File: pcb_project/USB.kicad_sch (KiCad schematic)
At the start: 6 parts, among them J2 USB_B_Mini, U2 TPS2041B

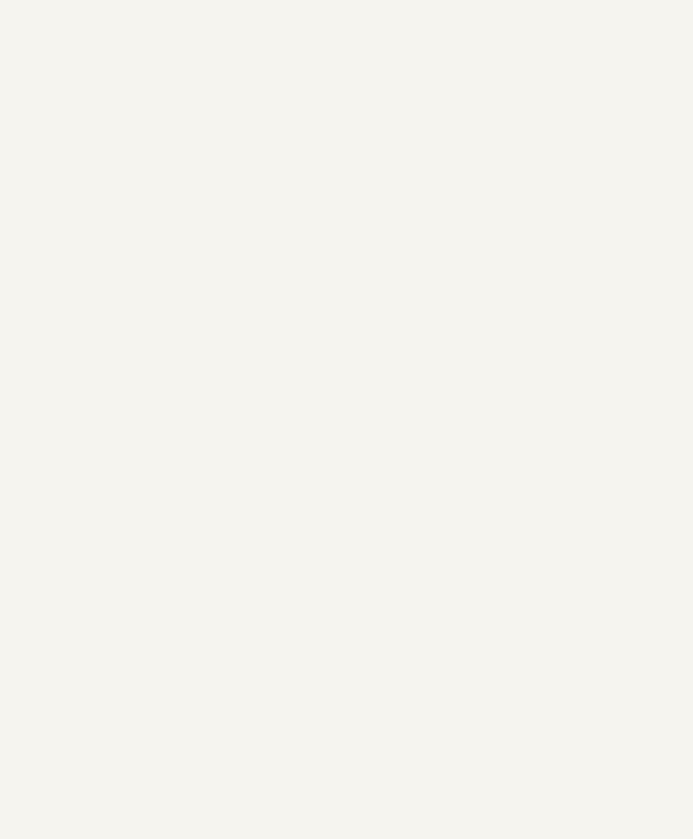
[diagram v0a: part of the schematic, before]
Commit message: Update USB circuits
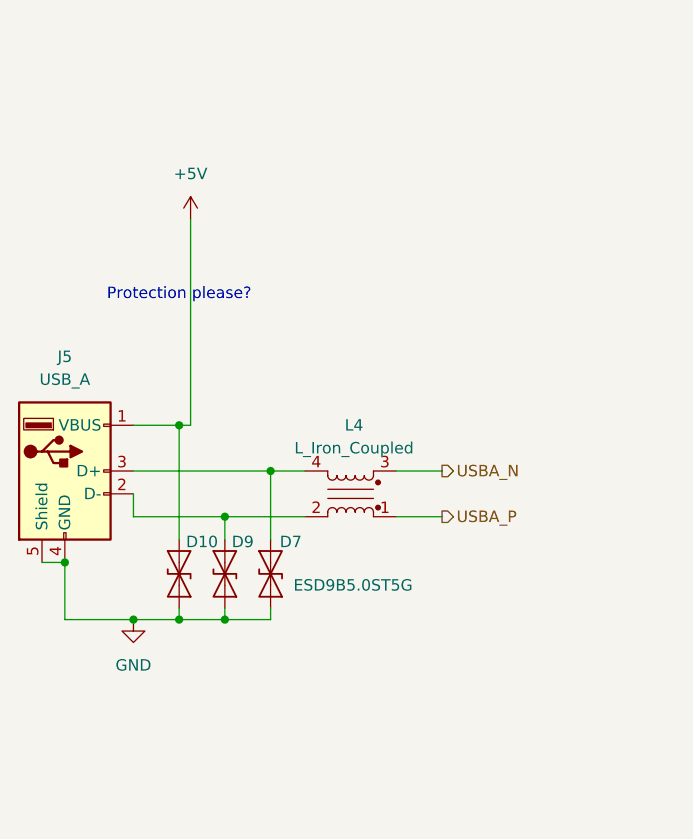
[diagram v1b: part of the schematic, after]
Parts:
- added D10, D7, D9: ESD9B5.0ST5G, Diode_SMD:D_SOD-923, symbol Diode:ESD9B5.0ST5G
- added J5: USB_A, symbol Connector:USB_A
- added L4: L_Iron_Coupled, symbol Device:L_Iron_Coupled
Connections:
- net GND: now also D10.1 (A1), D7.1 (A1), D9.1 (A1), J5.4 (GND), J5.5 (Shield)
- new net: D9.2 (A2), J5.2 (D-), L4.2
- new net: D7.2 (A2), J5.3 (D+), L4.4
- new net +5V: D10.2 (A2), J5.1 (VBUS)
- new net USBA_N: L4.3
- new net USBA_P: L4.1
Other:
- note added: "Protection please?"

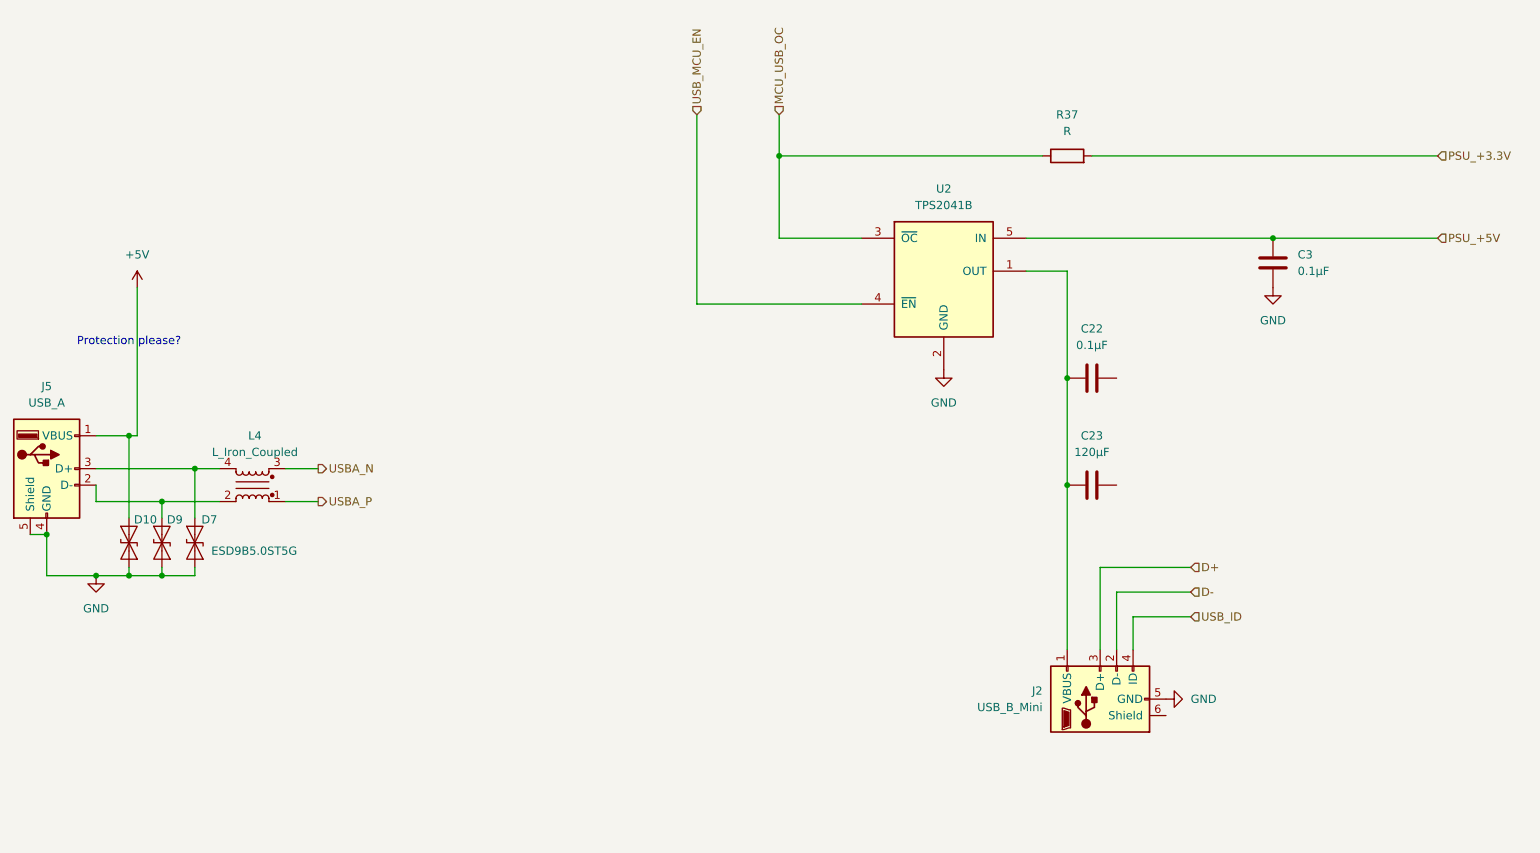
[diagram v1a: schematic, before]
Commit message: Update USB component and redo pin choices for MCU
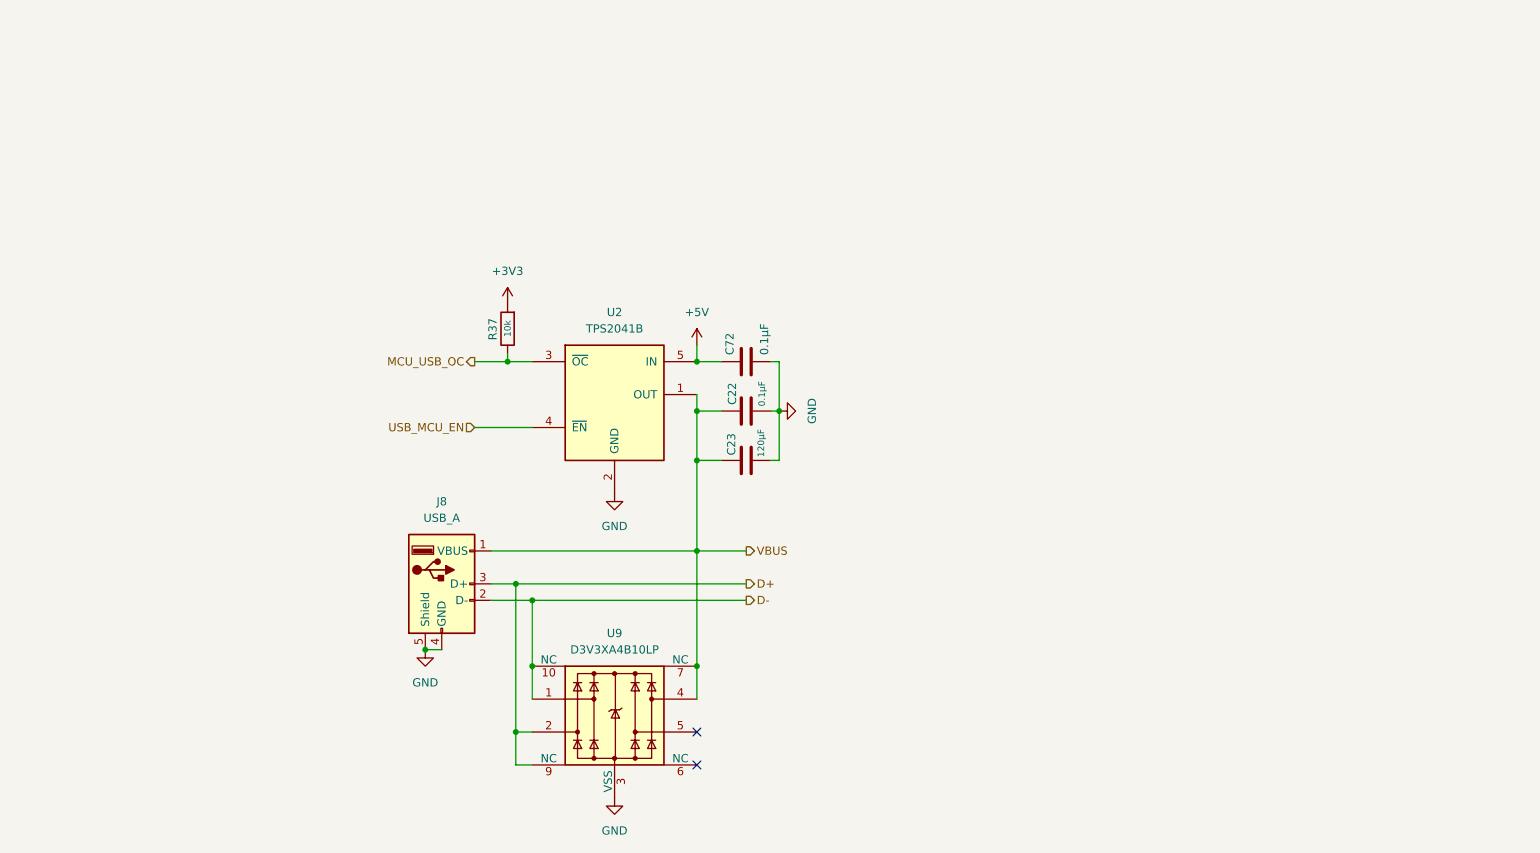
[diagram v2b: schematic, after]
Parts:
- removed C3: 0.1µF, symbol Device:C
- removed D10, D7, D9: ESD9B5.0ST5G, Diode_SMD:D_SOD-923, symbol Diode:ESD9B5.0ST5G
- removed J2: USB_B_Mini, symbol Connector:USB_B_Mini
- removed J5: USB_A, symbol Connector:USB_A
- removed L4: L_Iron_Coupled, symbol Device:L_Iron_Coupled
- added C72: 0.1μF, symbol Device:C
- added J8: USB_A, symbol Connector:USB_A
- added U9: D3V3XA4B10LP, Package_DFN_QFN:Diodes_UDFN-10_1.0x2.5mm_P0.5mm, symbol Power_Protection:D3V3XA4B10LP
- R37: value R -> 10k
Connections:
- net PSU_+5V is gone; now on net +5V: U2.5 (IN)
- net +5V: now also C72.1
- net D+: now also J8.3 (D+), U9.2, U9.9 (NC)
- net D-: now also J8.2 (D-), U9.1, U9.10 (NC)
- net GND: now also C22.1, C23.1, C72.2, J8.4 (GND), J8.5 (Shield), U9.3 (VSS), U9.8 (VSS)
- net VBUS: now reaches C22.2, C23.2, U2.1 (OUT)
- net VBUS: now also J8.1 (VBUS), U9.4, U9.7 (NC)
- net PSU_+3.3V renamed +3V3
- no-connect marks 0 -> 2
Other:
- note removed: "Protection please?"
- moved on the sheet: C22, C23, R37, U2

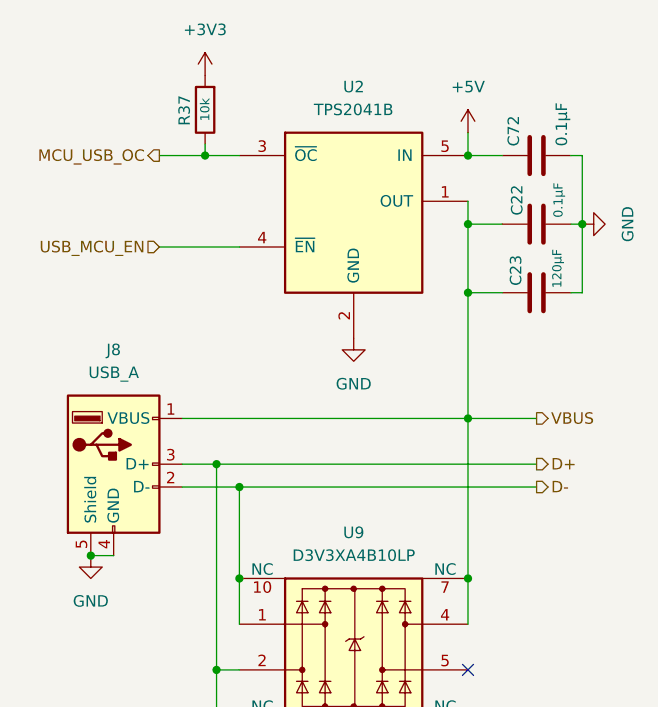
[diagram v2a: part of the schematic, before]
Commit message: ERC fixes, some remain
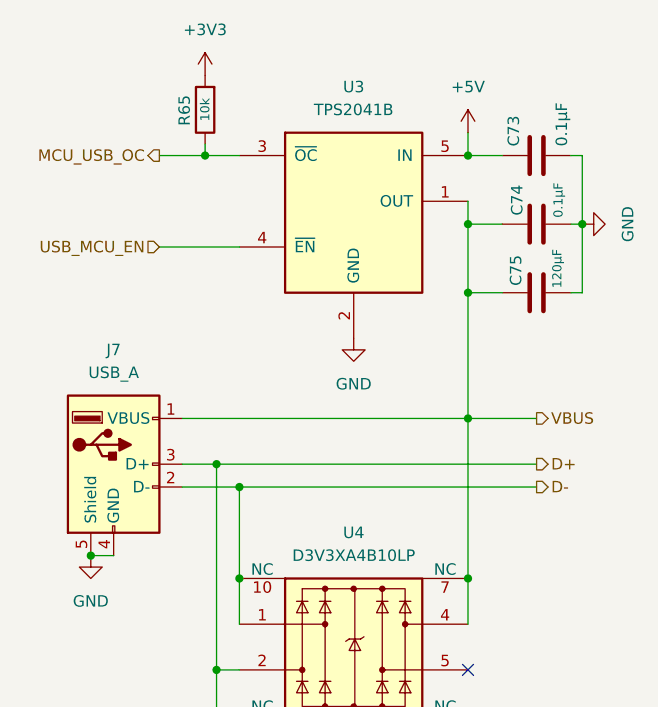
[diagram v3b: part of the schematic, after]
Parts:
- renumbered C72 to C73, C22 to C74, C23 to C75, J8 to J7, R37 to R65, U2 to U3, U9 to U4
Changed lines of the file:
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@@
 		(on_board yes)
 		(dnp no)
-		(property "Reference" "C22"
+		(property "Reference" "C74"
 			(at 145.161 74.803 0)
 			(effects
@@
 			(project ""
 				(path "/98f80f66-4595-4d0f-90ca-59b2db6f447b/d8354ada-74b3-4c6a-8679-c8f4ff1d8cd0"
-					(reference "C22")
+					(reference "C74")
 					(unit 1)
 				)
@@
 		(dnp no)
 		(fields_autoplaced yes)
-		(property "Reference" "#PWR011"
+		(property "Reference" "#PWR082"
 			(at 127 143.51 0)
 			(effects
@@
 			(project "pcb_project"
 				(path "/98f80f66-4595-4d0f-90ca-59b2db6f447b/d8354ada-74b3-4c6a-8679-c8f4ff1d8cd0"
-					(reference "#PWR011")
+					(reference "#PWR082")
 					(unit 1)
 				)
@@
 		(dnp no)
 		(fields_autoplaced yes)
-		(property "Reference" "U9"
+		(property "Reference" "U4"
 			(at 127 111.76 0)
 			(effects
@@
 			(project ""
 				(path "/98f80f66-4595-4d0f-90ca-59b2db6f447b/d8354ada-74b3-4c6a-8679-c8f4ff1d8cd0"
-					(reference "U9")
+					(reference "U4")
 					(unit 1)
 				)
@@
 		(on_board yes)
 		(dnp no)
-		(property "Reference" "R37"
+		(property "Reference" "R65"
 			(at 108.204 66.548 90)
 			(effects
@@
 			(project ""
 				(path "/98f80f66-4595-4d0f-90ca-59b2db6f447b/d8354ada-74b3-4c6a-8679-c8f4ff1d8cd0"
-					(reference "R37")
+					(reference "R65")
 					(unit 1)
 				)
@@
 		(dnp no)
 		(fields_autoplaced yes)
-		(property "Reference" "J8"
+		(property "Reference" "J7"
 			(at 100.33 91.44 0)
 			(effects
@@
 			(project "pcb_project"
 				(path "/98f80f66-4595-4d0f-90ca-59b2db6f447b/d8354ada-74b3-4c6a-8679-c8f4ff1d8cd0"
-					(reference "J8")
+					(reference "J7")
 					(unit 1)
 				)
@@
 		(on_board yes)
 		(dnp no)
-		(property "Reference" "C23"
+		(property "Reference" "C75"
 			(at 145.034 84.328 0)
 			(effects
@@
 			(project ""
 				(path "/98f80f66-4595-4d0f-90ca-59b2db6f447b/d8354ada-74b3-4c6a-8679-c8f4ff1d8cd0"
-					(reference "C23")
+					(reference "C75")
 					(unit 1)
 				)
@@
 		(dnp no)
 		(fields_autoplaced yes)
-		(property "Reference" "#PWR086"
+		(property "Reference" "#PWR079"
 			(at 97.79 120.65 0)
 			(effects
@@
 			(project "pcb_project"
 				(path "/98f80f66-4595-4d0f-90ca-59b2db6f447b/d8354ada-74b3-4c6a-8679-c8f4ff1d8cd0"
-					(reference "#PWR086")
+					(reference "#PWR079")
 					(unit 1)
 				)
@@
 		(dnp no)
 		(fields_autoplaced yes)
-		(property "Reference" "#PWR015"
+		(property "Reference" "#PWR084"
 			(at 158.75 77.47 0)
 			(effects
@@
 			(project "pcb_project"
 				(path "/98f80f66-4595-4d0f-90ca-59b2db6f447b/d8354ada-74b3-4c6a-8679-c8f4ff1d8cd0"
-					(reference "#PWR015")
+					(reference "#PWR084")
 					(unit 1)
 				)
@@
 		(dnp no)
 		(fields_autoplaced yes)
-		(property "Reference" "#PWR084"
+		(property "Reference" "#PWR083"
 			(at 139.7 71.12 0)
 			(effects
@@
 			(project ""
 				(path "/98f80f66-4595-4d0f-90ca-59b2db6f447b/d8354ada-74b3-4c6a-8679-c8f4ff1d8cd0"
-					(reference "#PWR084")
+					(reference "#PWR083")
 					(unit 1)
 				)
@@
 		(dnp no)
 		(fields_autoplaced yes)
-		(property "Reference" "#PWR013"
+		(property "Reference" "#PWR080"
 			(at 110.49 64.77 0)
 			(effects
@@
 			(project ""
 				(path "/98f80f66-4595-4d0f-90ca-59b2db6f447b/d8354ada-74b3-4c6a-8679-c8f4ff1d8cd0"
-					(reference "#PWR013")
+					(reference "#PWR080")
 					(unit 1)
 				)
@@
 		(on_board yes)
 		(dnp no)
-		(property "Reference" "C72"
+		(property "Reference" "C73"
 			(at 144.78 68.834 0)
 			(effects
@@
 			(project ""
 				(path "/98f80f66-4595-4d0f-90ca-59b2db6f447b/d8354ada-74b3-4c6a-8679-c8f4ff1d8cd0"
-					(reference "C72")
+					(reference "C73")
 					(unit 1)
 				)
@@
 		(dnp no)
 		(fields_autoplaced yes)
-		(property "Reference" "#PWR012"
+		(property "Reference" "#PWR081"
 			(at 127 96.52 0)
 			(effects
@@
 			(project ""
 				(path "/98f80f66-4595-4d0f-90ca-59b2db6f447b/d8354ada-74b3-4c6a-8679-c8f4ff1d8cd0"
-					(reference "#PWR012")
+					(reference "#PWR081")
 					(unit 1)
 				)
@@
 		(dnp no)
 		(fields_autoplaced yes)
-		(property "Reference" "U2"
+		(property "Reference" "U3"
 			(at 127 62.23 0)
 			(effects
@@
 			(project ""
 				(path "/98f80f66-4595-4d0f-90ca-59b2db6f447b/d8354ada-74b3-4c6a-8679-c8f4ff1d8cd0"
-					(reference "U2")
-					(unit 1)
-				)
+					(reference "U3")
+					(unit 1)
+				)

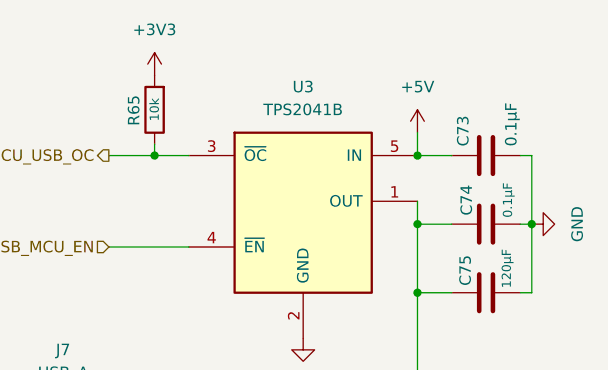
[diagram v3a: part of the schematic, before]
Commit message: Fix USB pins and other ERC errors
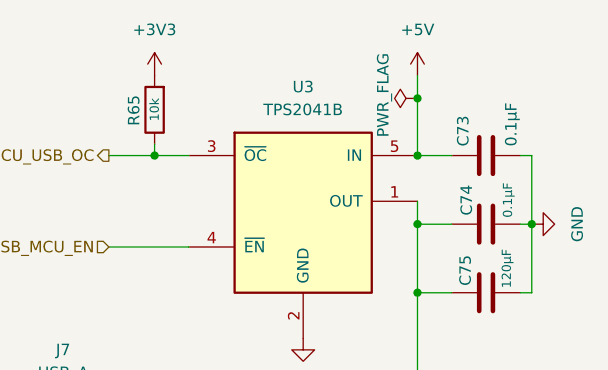
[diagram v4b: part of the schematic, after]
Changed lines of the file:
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@@
+	)
+	(junction
+		(at 139.7 63.5)
+		(diameter 0)
+		(color 0 0 0 0)
 	)
 	(junction
@@
 	(wire
 		(pts
-			(xy 139.7 67.31) (xy 139.7 69.85)
+			(xy 139.7 60.96) (xy 139.7 63.5)
 		)
 		(stroke
@@
 		(pts
 			(xy 111.76 127) (xy 111.76 132.08)
+		)
+		(stroke
+			(width 0)
+			(type default)
+		)
+	)
+	(wire
+		(pts
+			(xy 139.7 63.5) (xy 139.7 69.85)
 		)
 		(stroke
@@
 	(symbol
 		(lib_id "power:+5V")
-		(at 139.7 67.31 0)
+		(at 139.7 60.96 0)
 		(unit 1)
 		(exclude_from_sim no)
@@
 		(fields_autoplaced yes)
 		(property "Reference" "#PWR083"
-			(at 139.7 71.12 0)
+			(at 139.7 64.77 0)
 			(effects
 				(font
@@
 		)
 		(property "Value" "+5V"
-			(at 139.7 62.23 0)
+			(at 139.7 55.88 0)
 			(effects
 				(font
@@
 		)
 		(property "Footprint" ""
-			(at 139.7 67.31 0)
+			(at 139.7 60.96 0)
 			(effects
 				(font
@@
 		)
 		(property "Datasheet" ""
-			(at 139.7 67.31 0)
+			(at 139.7 60.96 0)
 			(effects
 				(font
@@
 		)
 		(property "Description" "Power symbol creates a global label with name \"+5V\""
-			(at 139.7 67.31 0)
+			(at 139.7 60.96 0)
 			(effects
 				(font
@@
 					(unit 1)
 				)
+			)
+		)
+	)
+	(symbol
+		(lib_id "power:PWR_FLAG")
+		(at 139.7 63.5 90)
+		(unit 1)
+		(exclude_from_sim no)
+		(in_bom yes)
+		(on_board yes)
+		(dnp no)
+		(property "Reference" "#FLG05"
+			(at 137.795 63.5 0)
+			(effects
+				(font
+					(size 1.27 1.27)
+				)
+				(hide yes)
+			)
+		)
+		(property "Value" "PWR_FLAG"
+			(at 135.89 67.818 0)
+			(effects
+				(font
+					(size 1.27 1.27)
+				)
+				(justify left)
+			)
+		)
+		(property "Footprint" ""
+			(at 139.7 63.5 0)
+			(effects
+				(font
+					(size 1.27 1.27)
+				)
+				(hide yes)
+			)
+		)
+		(property "Datasheet" "~"
+			(at 139.7 63.5 0)
+			(effects
+				(font
+					(size 1.27 1.27)
+				)
+				(hide yes)
+			)
+		)
+		(property "Description" "Special symbol for telling ERC where power comes from"
+			(at 139.7 63.5 0)
+			(effects
+				(font
+					(size 1.27 1.27)
+				)
+				(hide yes)
+			)
+		)
+		(pin "1"
+		)
+		(instances
+			(project ""
+				(path "/98f80f66-4595-4d0f-90ca-59b2db6f447b/d8354ada-74b3-4c6a-8679-c8f4ff1d8cd0"
+					(reference "#FLG05")
+					(unit 1)
+				)

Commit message: Add most footprints, missing some inductors and 3 buttons
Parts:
- C73, C74: footprint (none) -> Capacitor_SMD:C_0603_1608Metric_Pad1.08x0.95mm_HandSolder
- C75: footprint (none) -> Capacitor_SMD:CP_Elec_6.3x7.7
- J7: footprint (none) -> Connector_USB:USB_A_Wuerth_614004134726_Horizontal
- R65: footprint (none) -> Resistor_SMD:R_0805_2012Metric_Pad1.20x1.40mm_HandSolder
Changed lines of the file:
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@@
 			)
 		)
-		(property "Footprint" ""
+		(property "Footprint" "Capacitor_SMD:C_0603_1608Metric_Pad1.08x0.95mm_HandSolder"
 			(at 143.51 78.4352 0)
 			(effects
@@
 			)
 		)
-		(property "Footprint" ""
+		(property "Footprint" "Resistor_SMD:R_0805_2012Metric_Pad1.20x1.40mm_HandSolder"
 			(at 112.268 64.77 90)
 			(effects
@@
 			)
 		)
-		(property "Footprint" ""
+		(property "Footprint" "Connector_USB:USB_A_Wuerth_614004134726_Horizontal"
 			(at 104.14 105.41 0)
 			(effects
@@
 			)
 		)
-		(property "Footprint" ""
+		(property "Footprint" "Capacitor_SMD:CP_Elec_6.3x7.7"
 			(at 143.51 86.0552 0)
 			(effects
@@
 			)
 		)
-		(property "Footprint" ""
+		(property "Footprint" "Capacitor_SMD:C_0603_1608Metric_Pad1.08x0.95mm_HandSolder"
 			(at 151.13 68.8848 0)
 			(effects
